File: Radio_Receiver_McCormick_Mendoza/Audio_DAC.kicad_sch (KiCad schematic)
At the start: 8 parts, among them J35 3.5mm_Jack, U14 PCM5102A

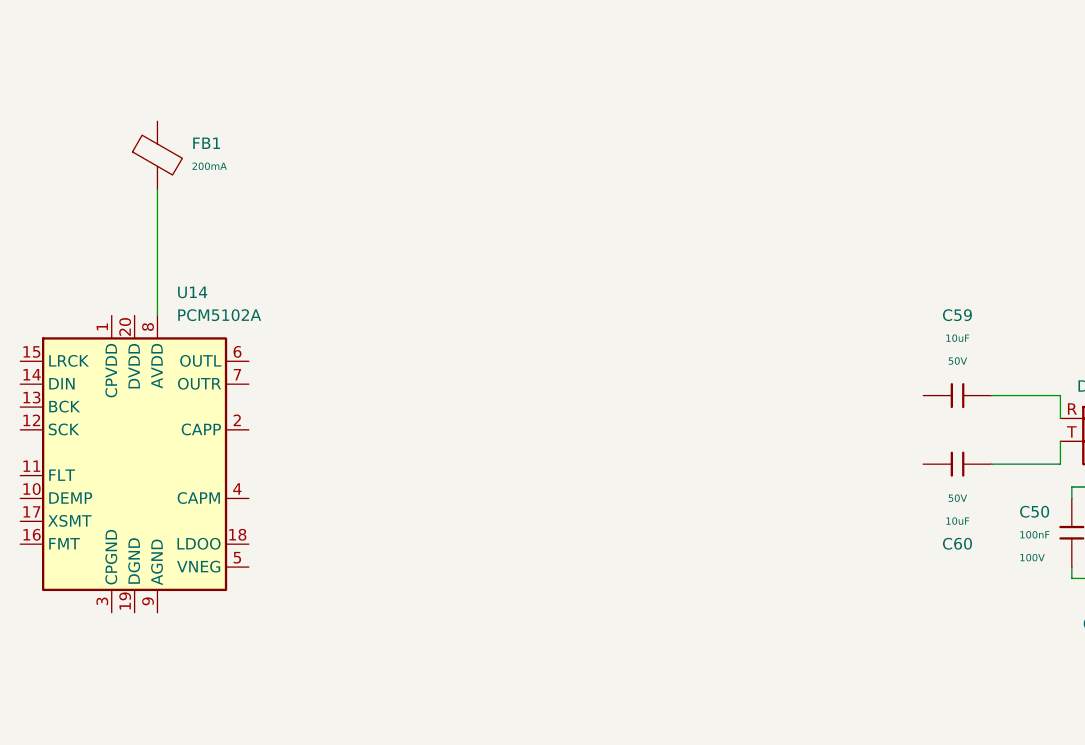
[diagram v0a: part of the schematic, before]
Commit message: Added digital power regulator
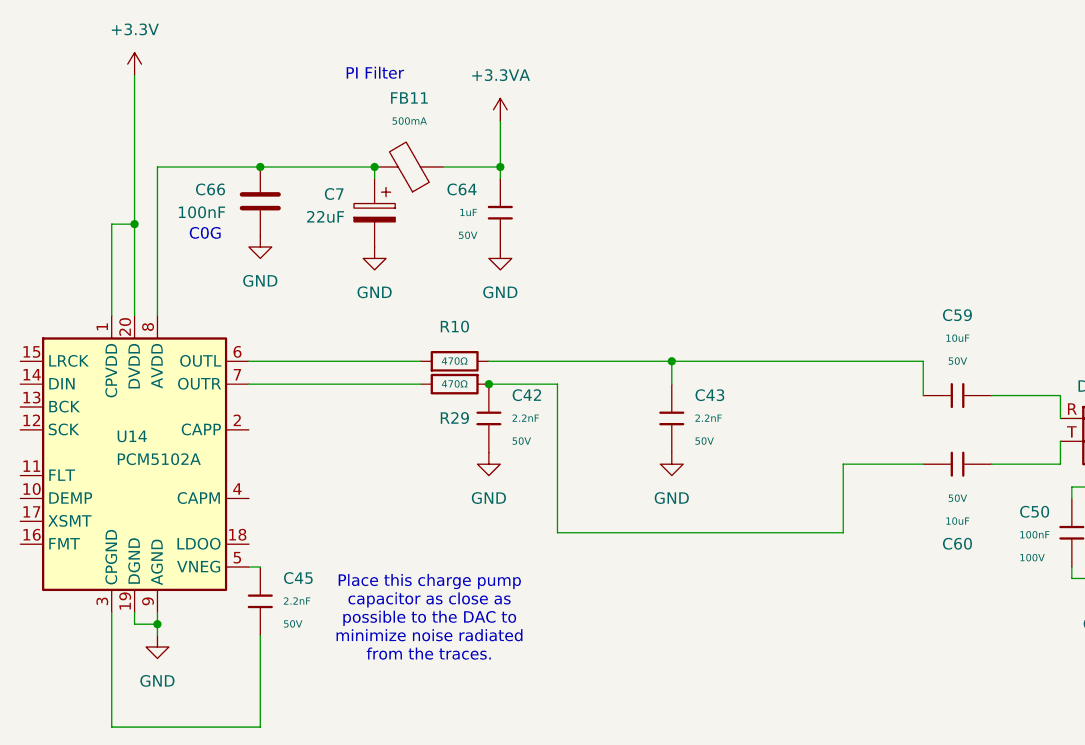
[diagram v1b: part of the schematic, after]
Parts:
- removed FB1: (no value), PCM_JLCPCB:FB_0603, symbol PCM_JLCPCB-Inductors:Ferrite,0603
- added C42, C43: 2.2nF, PCM_JLCPCB:C_0805, symbol PCM_JLCPCB-Capacitors:0805,2.2nF
- added C45: 2.2nF, PCM_JLCPCB:C_0603, symbol PCM_JLCPCB-Capacitors:0603,2.2nF
- added C64: 1uF, PCM_JLCPCB:C_0603, symbol PCM_JLCPCB-Capacitors:0603,1uF
- added C66: 100nF, PCM_JLCPCB:C_1206, symbol Device:C
- added C7: 22uF, PCM_JLCPCB:C_CASE-A-3216-18(mm), symbol Device:C_Polarized
- added FB11: (no value), PCM_JLCPCB:FB_0805, symbol PCM_JLCPCB-Inductors:Ferrite,0805,(2)
- added R10, R29: 470Ω, PCM_JLCPCB:R_0805, symbol PCM_JLCPCB-Resistors:0805,470Ω
- C50: Manufacturer Samsung Electro-Mechanics -> (none)
- C59, C60: Manufacturer Murata Electronics -> (none)
- R28: Manufacturer UNI-ROYAL(Uniroyal Elec) -> (none)
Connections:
- net at C59.1: now also C43.1, R10.2
- net +3.3V: now reaches U14.1 (CPVDD)
- net +3.3V: now also U14.20 (DVDD)
- net GND: now reaches U14.19 (DGND)
- net GND: now also U14.9 (AGND), C42.2, C43.2, C64.2, C66.2, C7.2
- net at U14.3 (CPGND): now also C45.2
- net at U14.5 (VNEG): now also C45.1
- net at U14.6 (OUTL): now also R10.1
- net at U14.7 (OUTR): now also R29.2
- net at U14.8 (AVDD): now also C66.1, C7.1, FB11.2
- net at C60.1: now also C42.1, R29.1
- new net +3.3VA: C64.1, FB11.1
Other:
- note added: "C0G"
- note added: "PI Filter"
- note added: "Place this charge pump capacitor as close as possible to the DAC to minimize noise radiated from the traces."

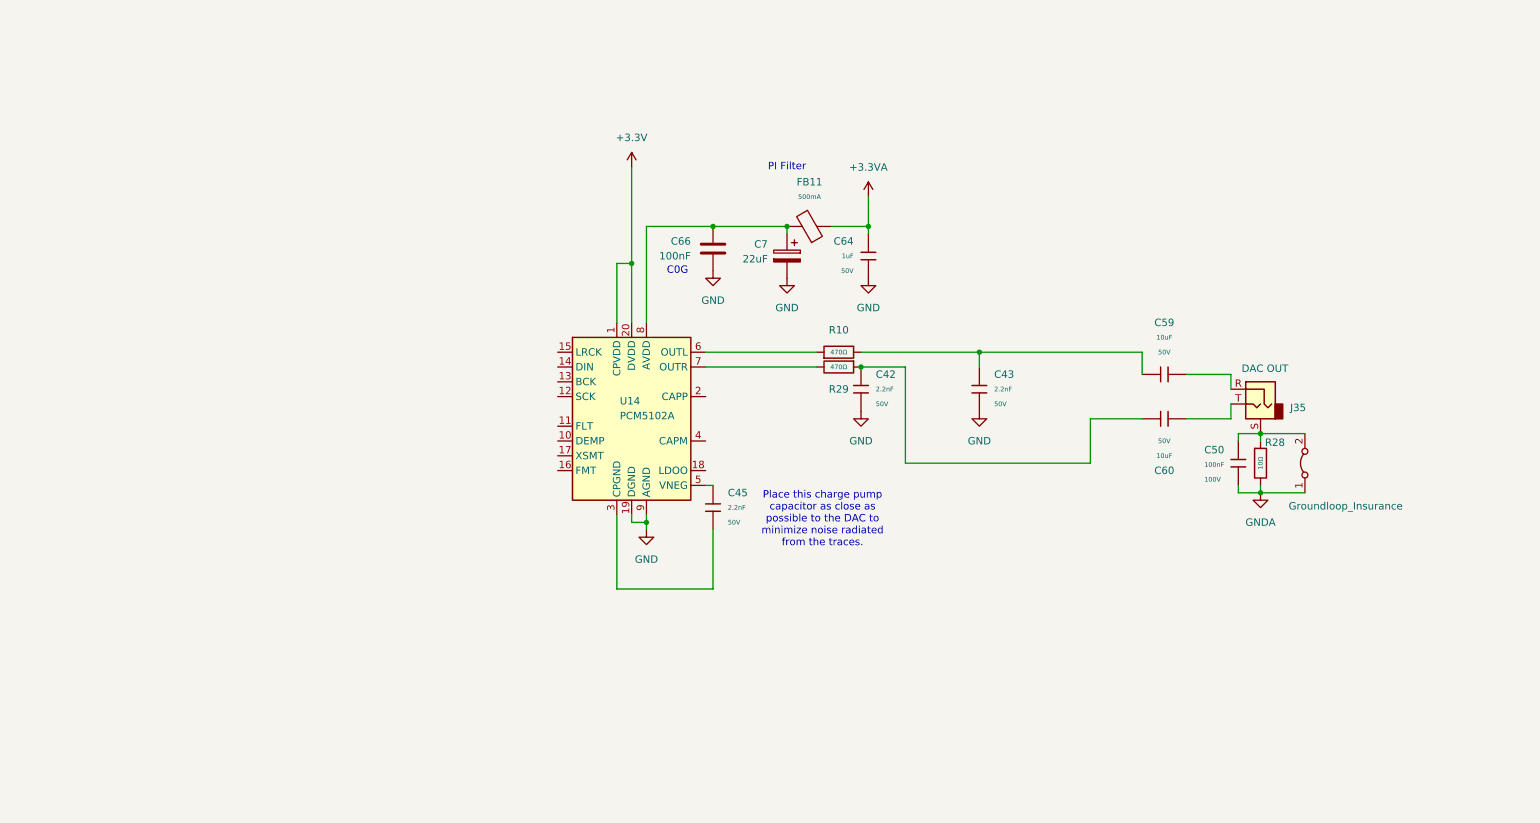
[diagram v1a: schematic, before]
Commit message: Integrated signal path modules
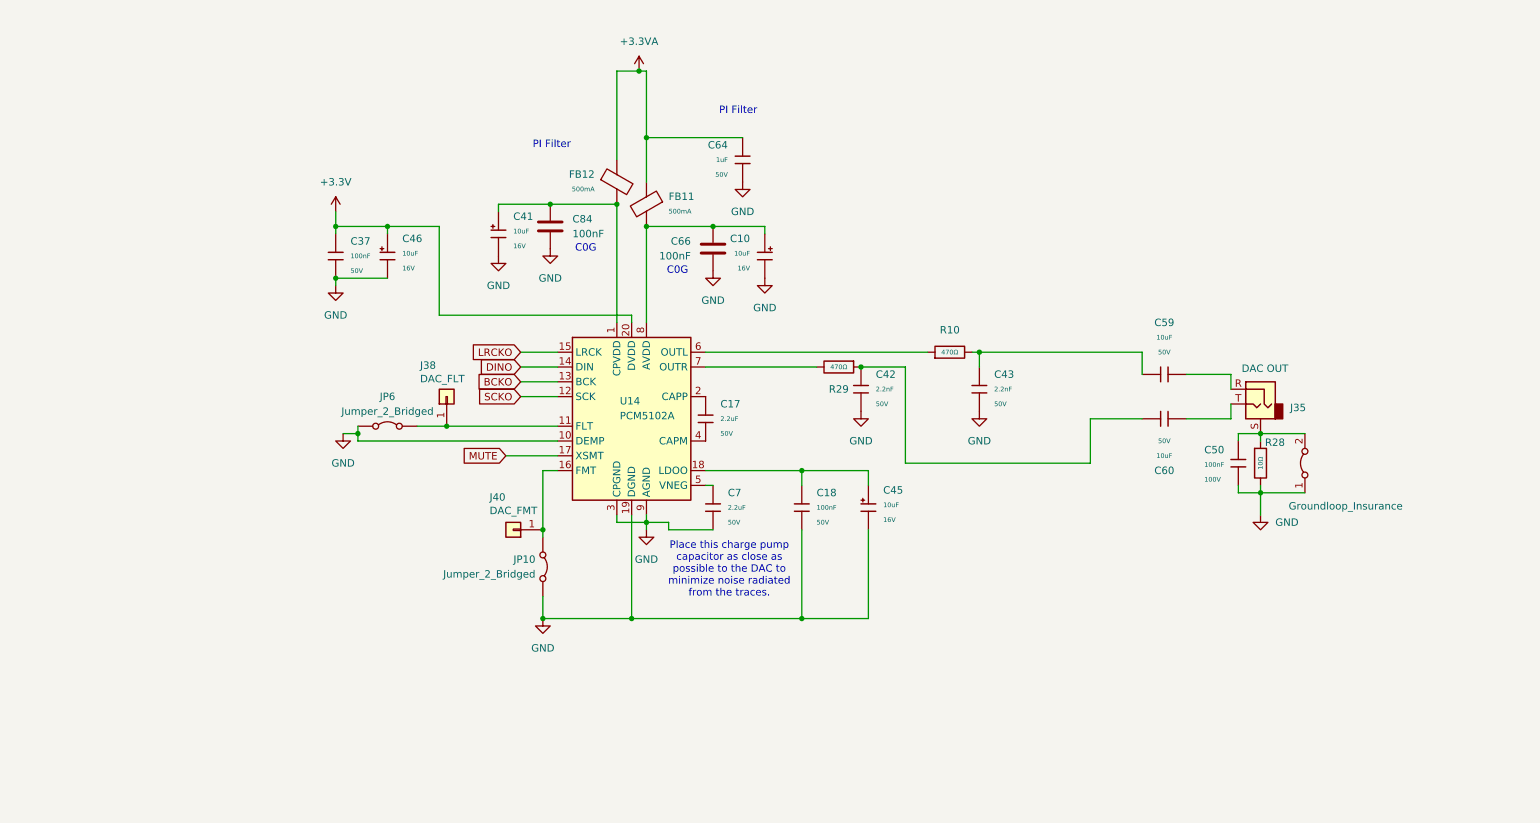
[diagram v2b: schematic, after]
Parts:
- removed C45: 2.2nF, PCM_JLCPCB:C_0603, symbol PCM_JLCPCB-Capacitors:0603,2.2nF
- removed C7: 22uF, PCM_JLCPCB:C_CASE-A-3216-18(mm), symbol Device:C_Polarized
- added C10, C41, C45, C46: 10uF, PCM_JLCPCB:C_CASE-A-3216-18(mm), symbol PCM_JLCPCB-Capacitors:CASE-A-3216-18(mm),10uF
- added C17, C7: 2.2uF, PCM_JLCPCB:C_0805, symbol PCM_JLCPCB-Capacitors:0805,2.2uF
- added C18, C37: 100nF, PCM_JLCPCB:C_0402, symbol PCM_JLCPCB-Capacitors:0402,100nF,(2)
- added C84: 100nF, PCM_JLCPCB:C_1206, symbol Device:C
- added FB12: (no value), PCM_JLCPCB:FB_0805, symbol PCM_JLCPCB-Inductors:Ferrite,0805,(2)
- added J38: DAC_FLT, Connector_PinHeader_2.54mm:PinHeader_1x01_P2.54mm_Vertical, symbol SDRReciever-rescue:Conn_01x01-Connector_Generic-SDRReciever-rescue
- added J40: DAC_FMT, Connector_PinHeader_2.54mm:PinHeader_1x01_P2.54mm_Vertical, symbol SDRReciever-rescue:Conn_01x01-Connector_Generic-SDRReciever-rescue
- added JP10, JP6: Jumper_2_Bridged, symbol Jumper:Jumper_2_Bridged
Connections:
- net GNDA is gone; now on net GND: C50.1, R28.2, e3.1 (A)
- net +3.3V: now also C37.1, C46.1; no longer U14.1 (CPVDD)
- net +3.3VA: now also FB12.1
- net GND: now also U14.10 (DEMP), U14.3 (CPGND), C10.2, C18.2, C37.2, C41.2, C45.2, C46.2, C7.2, C84.2, JP10.2 (B), JP6.1 (A)
- net at U14.5 (VNEG): now also C7.1
- net at U14.11 (FLT): now also J38.1 (Pin_1), JP6.2 (B)
- net SCKO: now reaches U14.12 (SCK)
- net BCKO: now reaches U14.13 (BCK)
- net DINO: now reaches U14.14 (DIN)
- net LRCKO: now reaches U14.15 (LRCK)
- net at U14.16 (FMT): now also J40.1 (Pin_1), JP10.1 (A)
- net MUTE: now reaches U14.17 (XSMT)
- net at U14.18 (LDOO): now also C18.1, C45.1
- net at U14.2 (CAPP): now also C17.2
- net at U14.4 (CAPM): now also C17.1
- net at C66.1, FB11.2, U14.8 (AVDD): now also C10.1
- new net: C41.1, C84.1, FB12.2, U14.1 (CPVDD)
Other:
- moved on the sheet: C64, FB11, R10

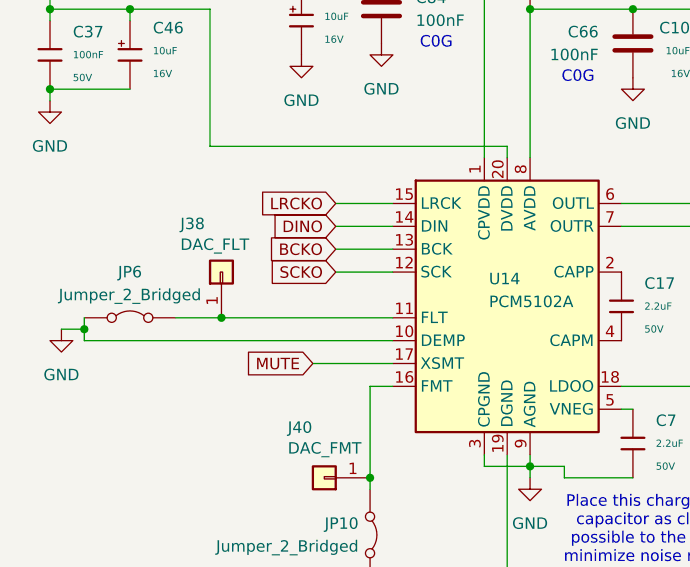
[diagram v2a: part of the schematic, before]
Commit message: Finalized Pico connections and added indicator LEDs
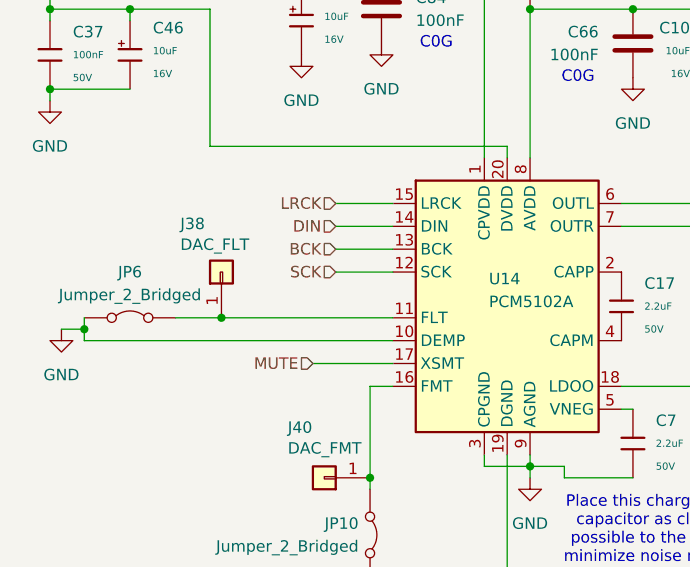
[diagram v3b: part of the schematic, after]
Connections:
- net BCKO renamed BCK
- net DINO renamed DIN
- net LRCKO renamed LRCK
- net SCKO renamed SCK
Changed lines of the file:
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@@
 		)
 	)
-	(global_label "LRCKO"
+	(hierarchical_label "SCK"
 		(shape input)
-		(at 107.95 78.74 180)
-		(fields_autoplaced yes)
+		(at 107.95 86.36 180)
 		(effects
 			(font
@@
 			(justify right)
 		)
-		(property "Intersheetrefs" "${INTERSHEET_REFS}"
-			(at 98.7962 78.74 0)
-			(hide yes)
-			(show_name no)
-			(do_not_autoplace no)
-			(effects
-				(font
-					(size 1.27 1.27)
-				)
-				(justify right)
-			)
-		)
 	)
-	(global_label "BCKO"
+	(hierarchical_label "DIN"
 		(shape input)
-		(at 107.95 83.82 180)
-		(fields_autoplaced yes)
+		(at 107.95 81.28 180)
 		(effects
 			(font
@@
 			(justify right)
 		)
-		(property "Intersheetrefs" "${INTERSHEET_REFS}"
-			(at 99.8243 83.82 0)
-			(hide yes)
-			(show_name no)
-			(do_not_autoplace no)
-			(effects
-				(font
-					(size 1.27 1.27)
-				)
-				(justify right)
-			)
-		)
 	)
-	(global_label "DINO"
+	(hierarchical_label "BCK"
 		(shape input)
-		(at 107.95 81.28 180)
-		(fields_autoplaced yes)
+		(at 107.95 83.82 180)
 		(effects
 			(font
@@
 			(justify right)
 		)
-		(property "Intersheetrefs" "${INTERSHEET_REFS}"
-			(at 100.429 81.28 0)
-			(hide yes)
-			(show_name no)
-			(do_not_autoplace no)
-			(effects
-				(font
-					(size 1.27 1.27)
-				)
-				(justify right)
-			)
-		)
 	)
-	(global_label "SCKO"
+	(hierarchical_label "LRCK"
 		(shape input)
-		(at 107.95 86.36 180)
-		(fields_autoplaced yes)
+		(at 107.95 78.74 180)
 		(effects
 			(font
@@
 			(justify right)
 		)
-		(property "Intersheetrefs" "${INTERSHEET_REFS}"
-			(at 99.8848 86.36 0)
-			(hide yes)
-			(show_name no)
-			(do_not_autoplace no)
-			(effects
-				(font
-					(size 1.27 1.27)
-				)
-				(justify right)
-			)
-		)
 	)
-	(global_label "MUTE"
+	(hierarchical_label "MUTE"
 		(shape input)
 		(at 105.41 96.52 180)
-		(fields_autoplaced yes)
 		(effects
 			(font
@@
 			(justify right)
 		)
-		(property "Intersheetrefs" "${INTERSHEET_REFS}"
-			(at 97.5263 96.52 0)
-			(hide yes)
-			(show_name no)
-			(do_not_autoplace no)
-			(effects
-				(font
-					(size 1.27 1.27)
-				)
-				(justify right)
-			)
-		)
 	)

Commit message: Added transformer footprint and datasheet
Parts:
- C10, C41, C45, C46: Manufacturer AVX -> (none)
- C17, C18, C37, C64, C7: Manufacturer Samsung Electro-Mechanics -> (none)
- FB11, FB12: Manufacturer Sunlord -> (none)
- U14: LCSC (none) -> C107671; Price (none) -> 4.0305USD
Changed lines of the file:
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@@
 			)
 		)
-		(property "Manufacturer" "AVX"
-			(at 104.14 58.42 0)
-			(hide yes)
-			(show_name no)
-			(do_not_autoplace no)
-			(effects
-				(font
-					(size 1.27 1.27)
-				)
-			)
-		)
 		(property "Part" "TAJA106K016RNJ"
 			(at 104.14 58.42 0)
@@
 			)
 		)
-		(property "Manufacturer" "Samsung Electro-Mechanics"
-			(at 140.97 105.41 0)
-			(hide yes)
-			(show_name no)
-			(do_not_autoplace no)
-			(effects
-				(font
-					(size 1.27 1.27)
-				)
-			)
-		)
 		(property "Part" "CL21A225KBQNNNE"
 			(at 140.97 105.41 0)
@@
 			)
 		)
-		(property "Manufacturer" "Samsung Electro-Mechanics"
-			(at 146.05 45.72 0)
-			(hide yes)
-			(show_name no)
-			(do_not_autoplace no)
-			(effects
-				(font
-					(size 1.27 1.27)
-				)
-			)
-		)
 		(property "Part" "CL10A105KB8NNNC"
 			(at 146.05 45.72 0)
@@
 			)
 		)
+		(property "LCSC" "C107671"
+			(at 127 88.9 0)
+			(hide yes)
+			(show_name no)
+			(do_not_autoplace no)
+			(effects
+				(font
+					(size 1.27 1.27)
+				)
+			)
+		)
+		(property "Price" "4.0305USD"
+			(at 127 88.9 0)
+			(hide yes)
+			(show_name no)
+			(do_not_autoplace no)
+			(effects
+				(font
+					(size 1.27 1.27)
+				)
+			)
+		)
 		(pin "5"
 		)
@@
 			)
 		)
-		(property "Manufacturer" "Sunlord"
-			(at 129.54 53.34 0)
-			(hide yes)
-			(show_name no)
-			(do_not_autoplace no)
-			(effects
-				(font
-					(size 1.27 1.27)
-				)
-			)
-		)
 		(property "Part" "GZ2012D601TF"
 			(at 129.54 53.34 0)
@@
 			)
 		)
-		(property "Manufacturer" "Samsung Electro-Mechanics"
-			(at 76.2 62.23 0)
-			(hide yes)
-			(show_name no)
-			(do_not_autoplace no)
-			(effects
-				(font
-					(size 1.27 1.27)
-				)
-			)
-		)
 		(property "Part" "CL05B104KB54PNC"
 			(at 76.2 62.23 0)
@@
 			)
 		)
-		(property "Manufacturer" "AVX"
-			(at 149.86 62.23 0)
-			(hide yes)
-			(show_name no)
-			(do_not_autoplace no)
-			(effects
-				(font
-					(size 1.27 1.27)
-				)
-			)
-		)
 		(property "Part" "TAJA106K016RNJ"
 			(at 149.86 62.23 0)
@@
 			)
 		)
-		(property "Manufacturer" "AVX"
-			(at 167.64 105.41 0)
-			(hide yes)
-			(show_name no)
-			(do_not_autoplace no)
-			(effects
-				(font
-					(size 1.27 1.27)
-				)
-			)
-		)
 		(property "Part" "TAJA106K016RNJ"
 			(at 167.64 105.41 0)
@@
 			)
 		)
-		(property "Manufacturer" "AVX"
-			(at 85.09 62.23 0)
-			(hide yes)
-			(show_name no)
-			(do_not_autoplace no)
-			(effects
-				(font
-					(size 1.27 1.27)
-				)
-			)
-		)
 		(property "Part" "TAJA106K016RNJ"
 			(at 85.09 62.23 0)
@@
 			)
 		)
-		(property "Manufacturer" "Sunlord"
-			(at 124.46 49.53 0)
-			(hide yes)
-			(show_name no)
-			(do_not_autoplace no)
-			(effects
-				(font
-					(size 1.27 1.27)
-				)
-			)
-		)
 		(property "Part" "GZ2012D601TF"
 			(at 124.46 49.53 0)
@@
 			)
 		)
-		(property "Manufacturer" "Samsung Electro-Mechanics"
-			(at 156.21 105.41 0)
-			(hide yes)
-			(show_name no)
-			(do_not_autoplace no)
-			(effects
-				(font
-					(size 1.27 1.27)
-				)
-			)
-		)
 		(property "Part" "CL05B104KB54PNC"
 			(at 156.21 105.41 0)
@@
 			(at 139.7 90.17 0)
 			(hide yes)
-			(show_name no)
-			(do_not_autoplace no)
-			(effects
-				(font
-					(size 1.27 1.27)
-				)
-			)
-		)
-		(property "Manufacturer" "Samsung Electro-Mechanics"
-			(at 139.7 90.17 0)
-			(hide yes)
